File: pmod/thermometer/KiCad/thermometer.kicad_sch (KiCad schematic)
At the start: 3 parts, among them J1 Conn_01x06_Pin, U1 DS18B20

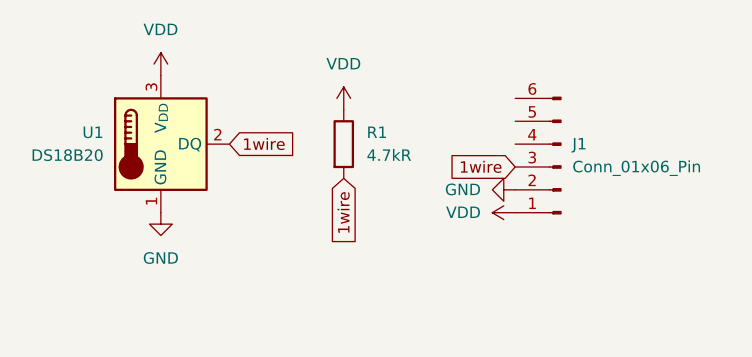
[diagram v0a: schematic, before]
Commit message: add M3 mounting hole
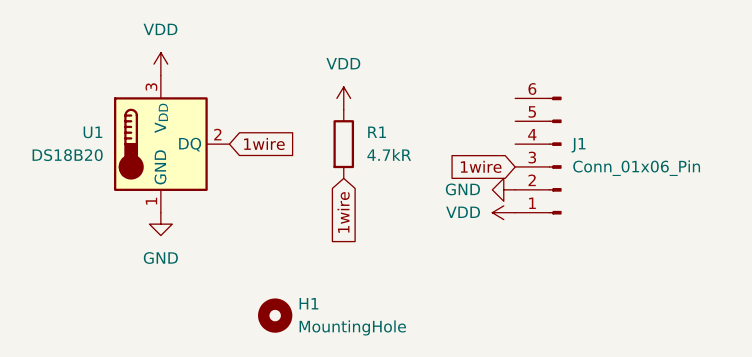
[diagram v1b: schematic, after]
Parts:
- added H1: MountingHole, MountingHole:MountingHole_3.2mm_M3, symbol Mechanical:MountingHole
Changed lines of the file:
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@@
+	)
+	(symbol
+		(lib_id "Mechanical:MountingHole")
+		(at 105.41 113.03 0)
+		(unit 1)
+		(exclude_from_sim no)
+		(in_bom no)
+		(on_board yes)
+		(dnp no)
+		(fields_autoplaced yes)
+		(property "Reference" "H1"
+			(at 107.95 111.7599 0)
+			(effects
+				(font
+					(size 1.27 1.27)
+				)
+				(justify left)
+			)
+		)
+		(property "Value" "MountingHole"
+			(at 107.95 114.2999 0)
+			(effects
+				(font
+					(size 1.27 1.27)
+				)
+				(justify left)
+			)
+		)
+		(property "Footprint" "MountingHole:MountingHole_3.2mm_M3"
+			(at 105.41 113.03 0)
+			(effects
+				(font
+					(size 1.27 1.27)
+				)
+				(hide yes)
+			)
+		)
+		(property "Datasheet" "~"
+			(at 105.41 113.03 0)
+			(effects
+				(font
+					(size 1.27 1.27)
+				)
+				(hide yes)
+			)
+		)
+		(property "Description" "Mounting Hole without connection"
+			(at 105.41 113.03 0)
+			(effects
+				(font
+					(size 1.27 1.27)
+				)
+				(hide yes)
+			)
+		)
+		(instances
+			(project ""
+				(path "/c7b5f5ba-a3a5-41ac-8d4c-ad3f1572fad6"
+					(reference "H1")
+					(unit 1)
+				)
+			)
+		)
 	)
 	(symbol
